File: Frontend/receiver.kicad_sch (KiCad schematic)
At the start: 0 parts

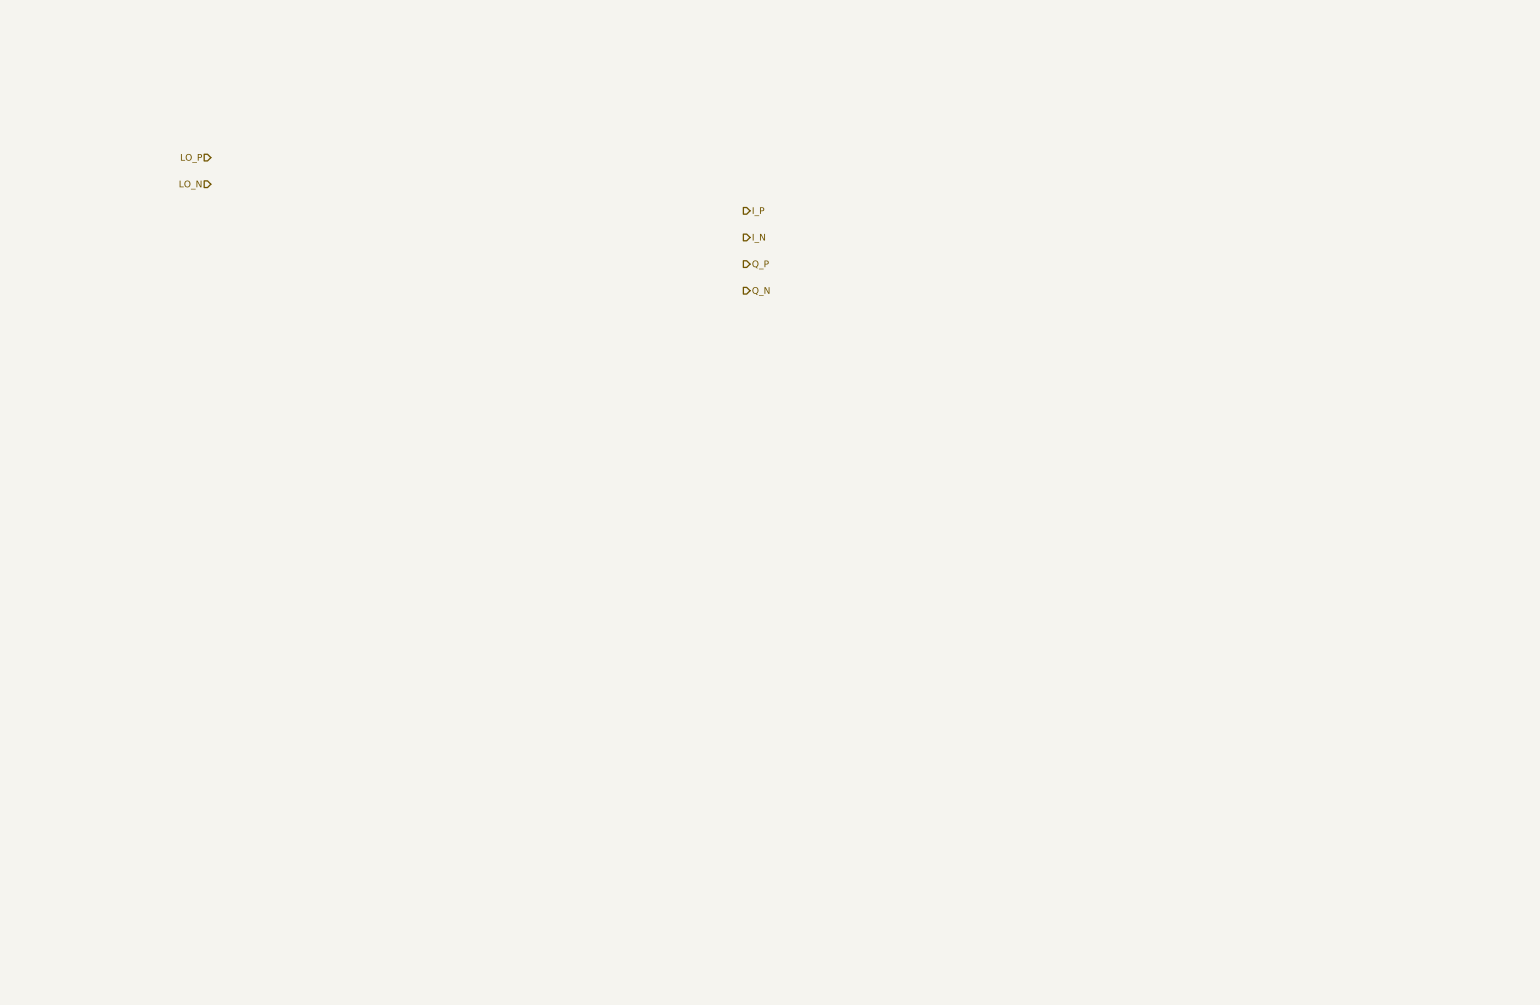
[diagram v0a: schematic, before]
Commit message: floorplan PCB some, draw out I/Q and VCO schematics
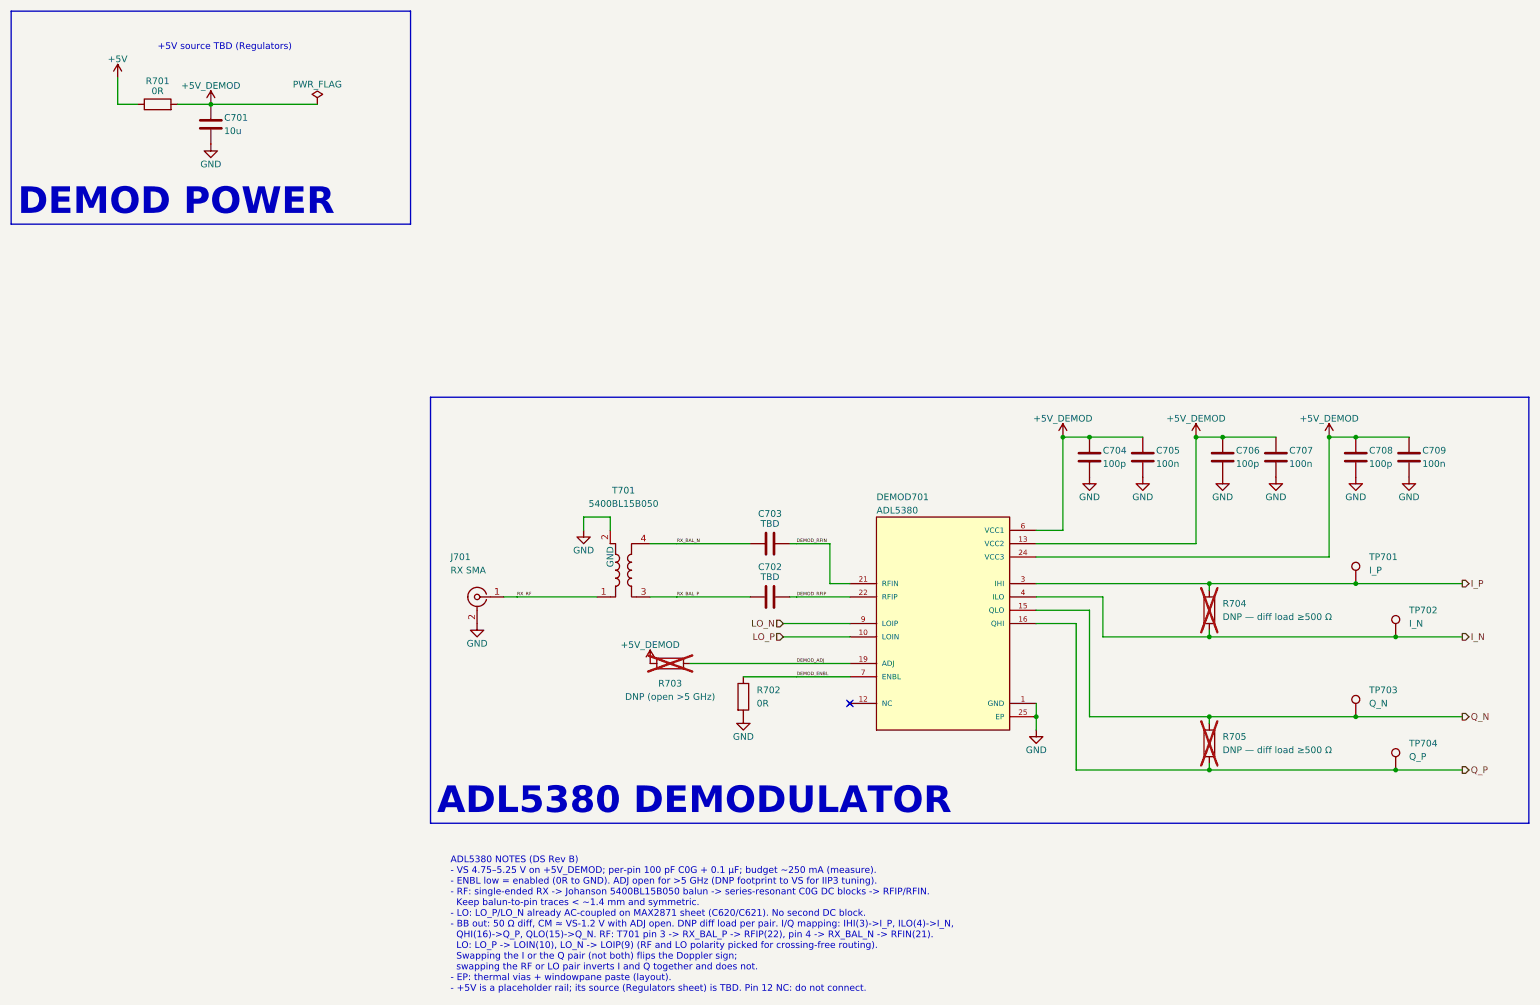
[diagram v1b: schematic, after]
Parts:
- added C701: 10u, Capacitor_SMD:C_0805_2012Metric, symbol cwradar:10u
- added C702, C703: TBD, Capacitor_SMD:C_0402_1005Metric, symbol Device:C
- added C704, C706, C708: 100p, Capacitor_SMD:C_0402_1005Metric, symbol cwradar:100p
- added C705, C707, C709: 100n, Capacitor_SMD:C_0402_1005Metric, symbol cwradar:100n
- added DEMOD701: ADL5380, cwradar:24-WFQFN, symbol cwradar:ADL5380ACPZ-R7
- added J701: RX SMA, Connector_Coaxial:SMA_Molex_73251-1153_EdgeMount_Horizontal, symbol Connector:Conn_Coaxial
- added R701: 0R, Resistor_SMD:R_0603_1608Metric, symbol cwradar:0R
- added R702: 0R, Resistor_SMD:R_0402_1005Metric, symbol cwradar:0R_0402
- added R703: DNP (open >5 GHz), Resistor_SMD:R_0402_1005Metric, symbol Device:R
- added R704, R705: DNP — diff load ≥500 Ω, Resistor_SMD:R_0402_1005Metric, symbol Device:R
- added T701: 5400BL15B050, RF_Converter:Balun_Johanson_5400BL15B050E, symbol cwradar:5400BL15B050
- added TP701: I_P, TestPoint:TestPoint_Pad_D1.0mm, symbol Connector:TestPoint
- added TP702: I_N, TestPoint:TestPoint_Pad_D1.0mm, symbol Connector:TestPoint
- added TP703: Q_N, TestPoint:TestPoint_Pad_D1.0mm, symbol Connector:TestPoint
- added TP704: Q_P, TestPoint:TestPoint_Pad_D1.0mm, symbol Connector:TestPoint
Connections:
- net I_N: now also DEMOD701.4 (ILO), R704.2, TP702.1
- net I_P: now also DEMOD701.3 (IHI), R704.1, TP701.1
- net LO_N: now also DEMOD701.9 (LOIP)
- net LO_P: now also DEMOD701.10 (LOIN)
- net Q_N: now also DEMOD701.15 (QLO), R705.1, TP703.1
- net Q_P: now also DEMOD701.16 (QHI), R705.2, TP704.1
- new net +5V: R701.1
- new net +5V_DEMOD: C701.1, C704.1, C705.1, C706.1, C707.1, C708.1, C709.1, DEMOD701.13 (VCC2), DEMOD701.24 (VCC3), DEMOD701.6 (VCC1), R701.2, R703.1
- new net DEMOD_ADJ: DEMOD701.19 (ADJ), R703.2
- new net DEMOD_ENBL: DEMOD701.7 (ENBL), R702.1
- new net DEMOD_RFIN: C703.2, DEMOD701.21 (RFIN)
- new net DEMOD_RFIP: C702.2, DEMOD701.22 (RFIP)
- new net GND: C701.2, C704.2, C705.2, C706.2, C707.2, C708.2, C709.2, DEMOD701.1 (GND), DEMOD701.11 (GND), DEMOD701.14 (GND), DEMOD701.17 (GND), DEMOD701.18 (GND), DEMOD701.2 (GND), DEMOD701.20 (GND), DEMOD701.23 (GND), DEMOD701.25 (EP), DEMOD701.25_1 (EP), DEMOD701.25_2 (EP), DEMOD701.25_3 (EP), DEMOD701.25_4 (EP), DEMOD701.25_5 (EP), DEMOD701.25_6 (EP), DEMOD701.25_7 (EP), DEMOD701.25_8 (EP), DEMOD701.25_9 (EP), DEMOD701.5 (GND), DEMOD701.8 (GND), J701.2 (Ext), R702.2, T701.2 (GND), T701.5 (GND)
- new net RX_BAL_N: C703.1, T701.4
- new net RX_BAL_P: C702.1, T701.3
- new net RX_RF: J701.1 (In), T701.1
- no-connect marks 0 -> 1
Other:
- note added: "+5V source TBD (Regulators)"
- note added: "ADL5380 DEMODULATOR"
- note added: "ADL5380 NOTES (DS Rev B) - VS 4.75–5.25 V on +5V_DEMOD; per-pin 100 pF C0G + 0.1 µF; budget ~250 mA (measure). - ENBL low = enabled (0R to GND). ADJ open for >5 GHz (DNP footprint to VS for IIP3 tuning). - RF: single-ended RX -> Johanson 5400BL15B050 balun -> series-resonant C0G DC blocks -> RFIP/RFIN. Keep balun-to-pin traces < ~1.4 mm and symmetric. - LO: LO_P/LO_N already AC-coupled on MAX2871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"
- note added: "DEMOD POWER"
